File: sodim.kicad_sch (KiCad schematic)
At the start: 7 parts, among them J1 Edge_Conn_Bus_DDR5_SODIMM_1xD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, U7 AT24CS01_SOT23

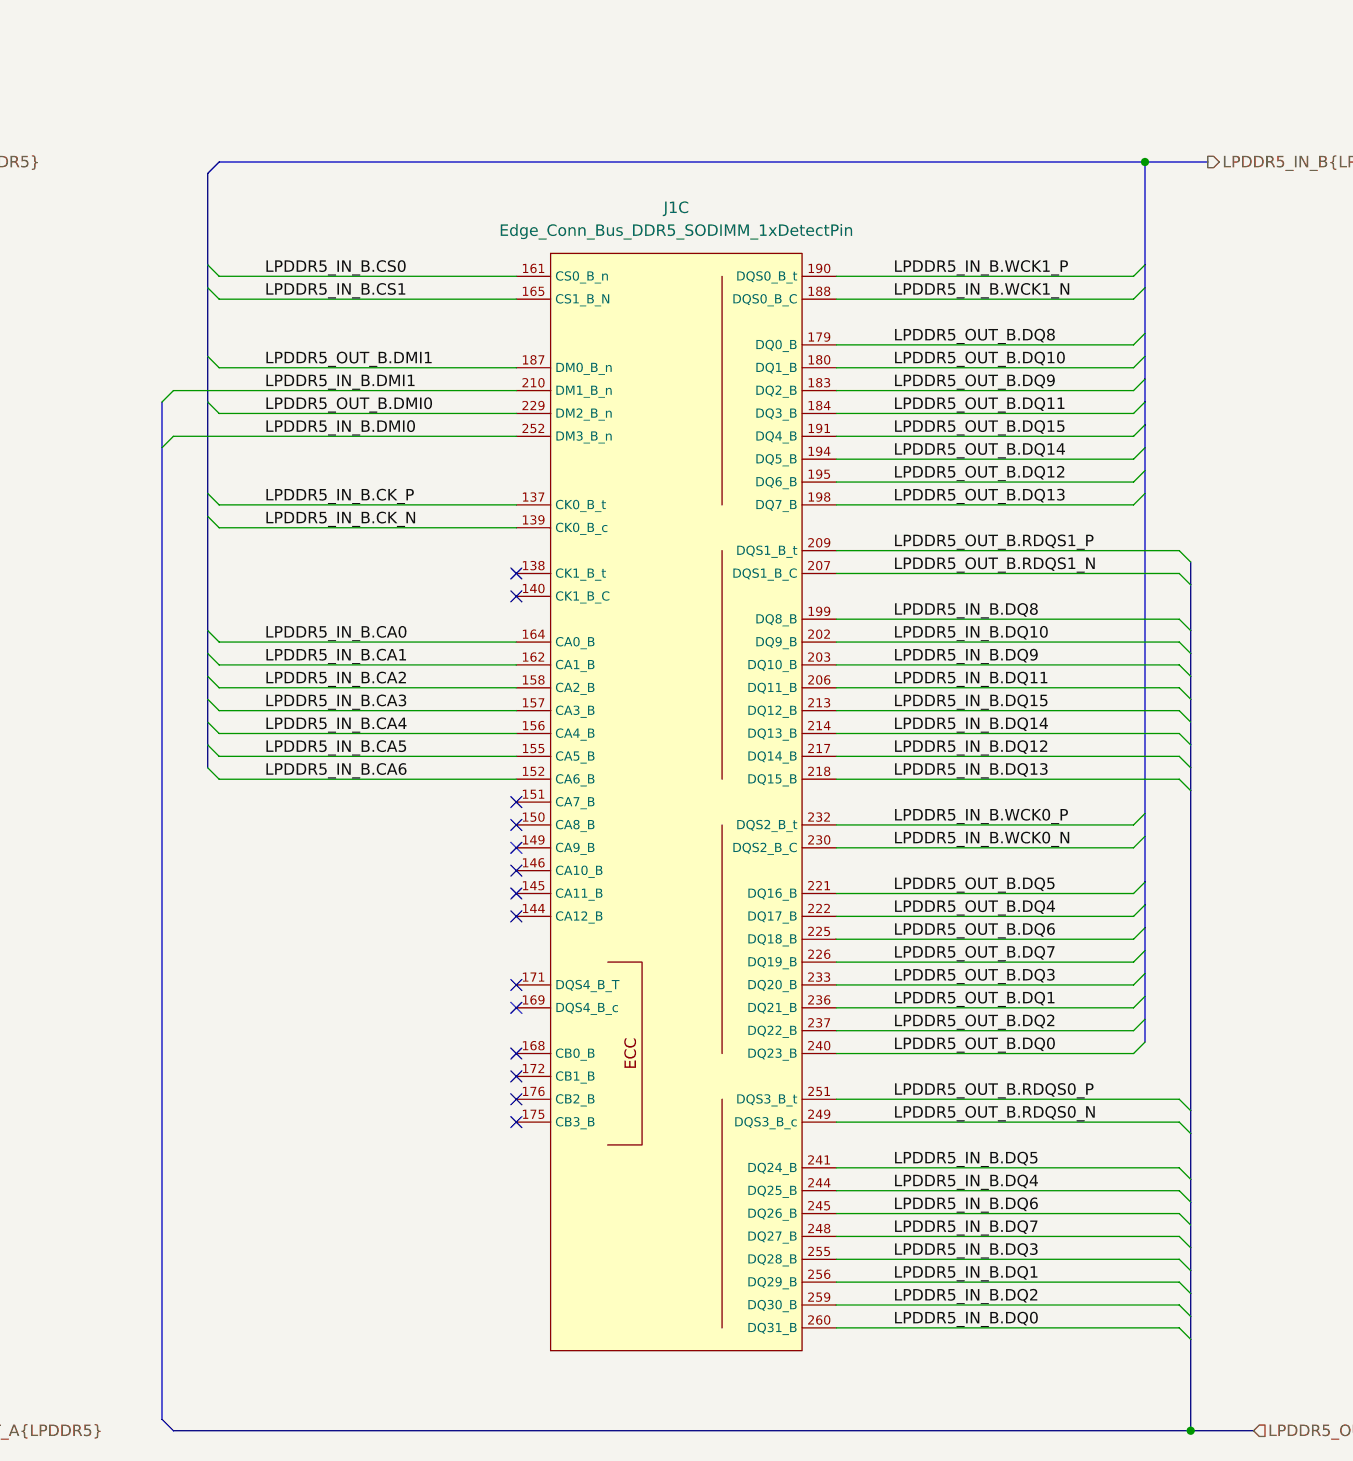
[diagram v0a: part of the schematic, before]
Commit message: [#53267] schematic: fix bus connections
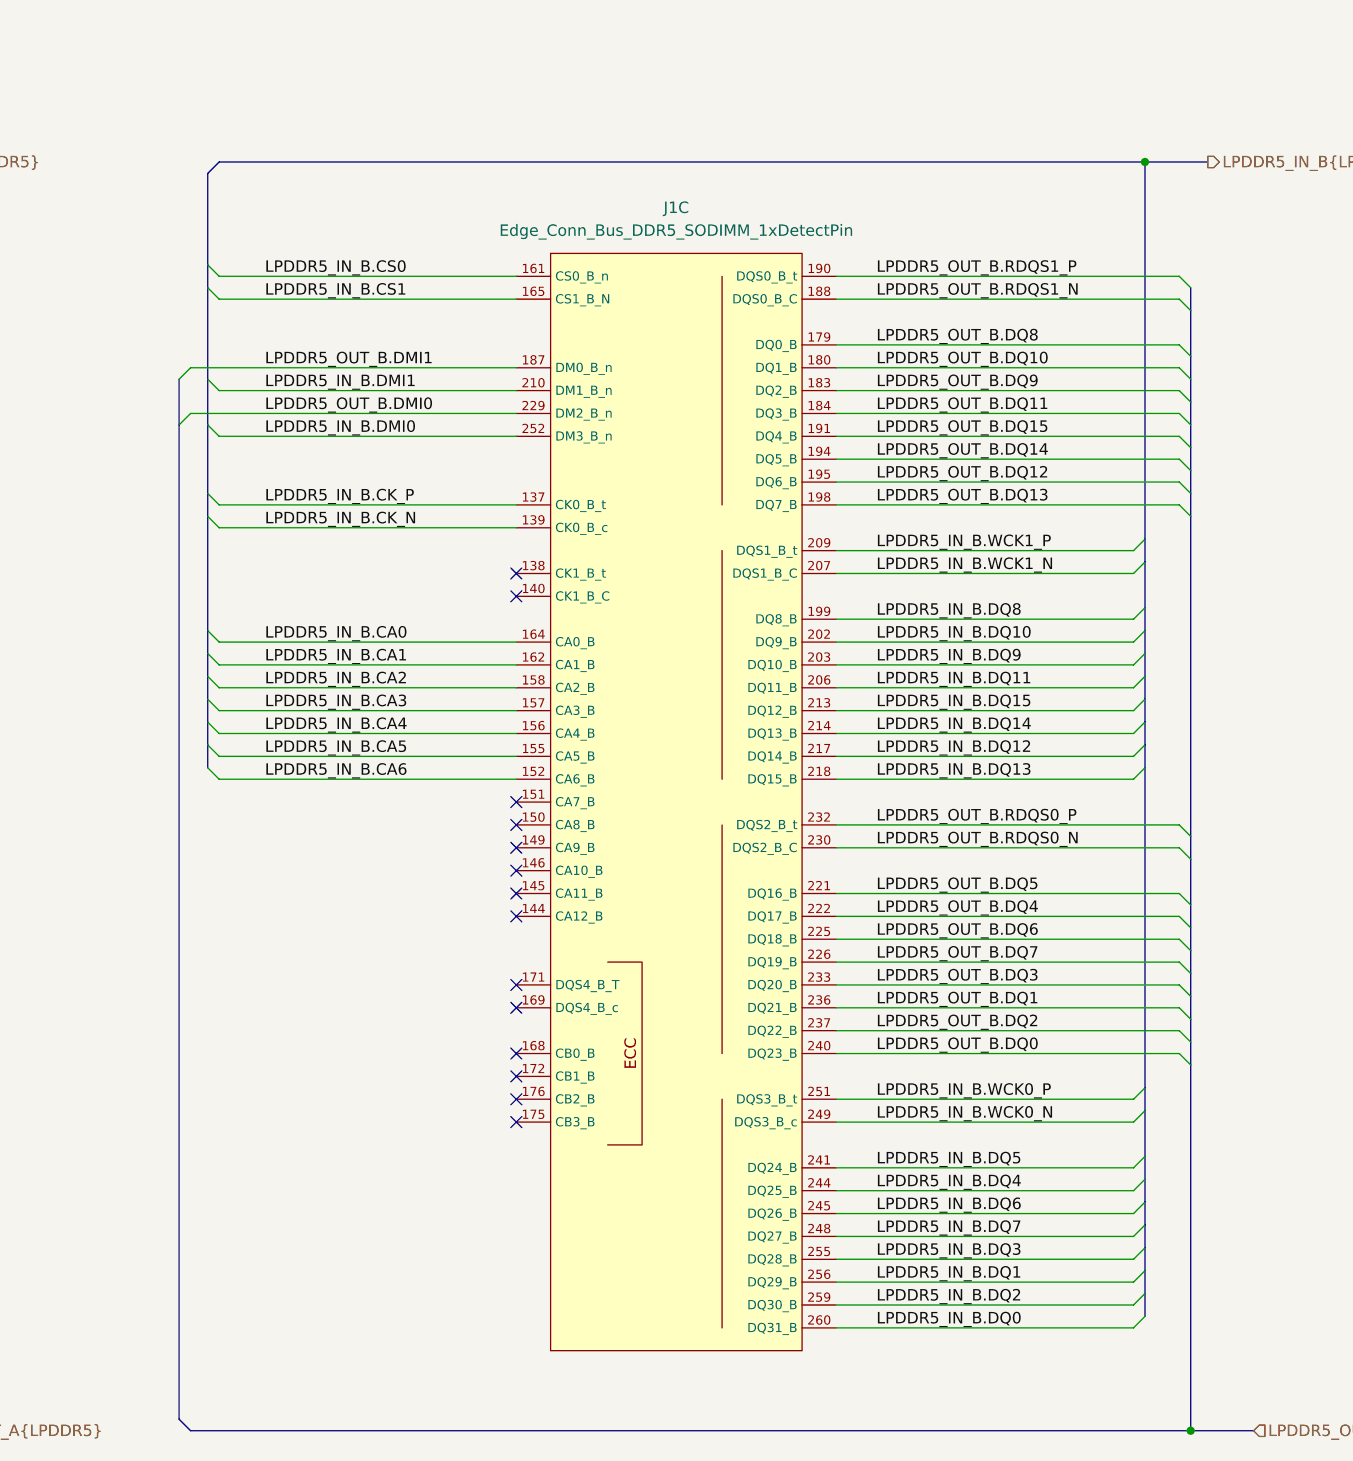
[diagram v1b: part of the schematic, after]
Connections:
- net LPDDR5_IN_B.WCK0_N: now also J1.249 (DQS3_B_c); no longer J1.230 (DQS2_B_C)
- net LPDDR5_IN_B.WCK0_P: now also J1.251 (DQS3_B_t); no longer J1.232 (DQS2_B_t)
- net LPDDR5_IN_B.WCK1_N: now also J1.207 (DQS1_B_C); no longer J1.188 (DQS0_B_C)
- net LPDDR5_IN_B.WCK1_P: now also J1.209 (DQS1_B_t); no longer J1.190 (DQS0_B_t)
- net LPDDR5_OUT_B.RDQS0_N: now also J1.230 (DQS2_B_C); no longer J1.249 (DQS3_B_c)
- net LPDDR5_OUT_B.RDQS0_P: now also J1.232 (DQS2_B_t); no longer J1.251 (DQS3_B_t)
- net LPDDR5_OUT_B.RDQS1_N: now also J1.188 (DQS0_B_C); no longer J1.207 (DQS1_B_C)
- net LPDDR5_OUT_B.RDQS1_P: now also J1.190 (DQS0_B_t); no longer J1.209 (DQS1_B_t)

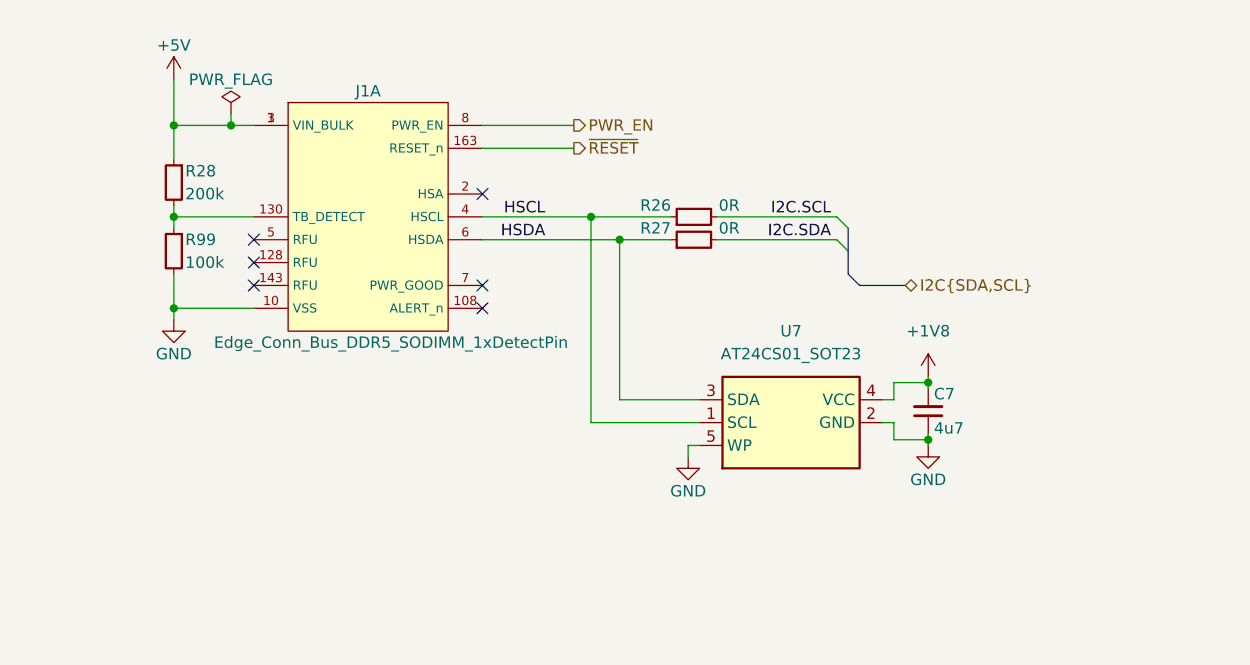
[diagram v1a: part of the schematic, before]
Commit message: [#53267] schematic: improve power supply sequencing and power good signal
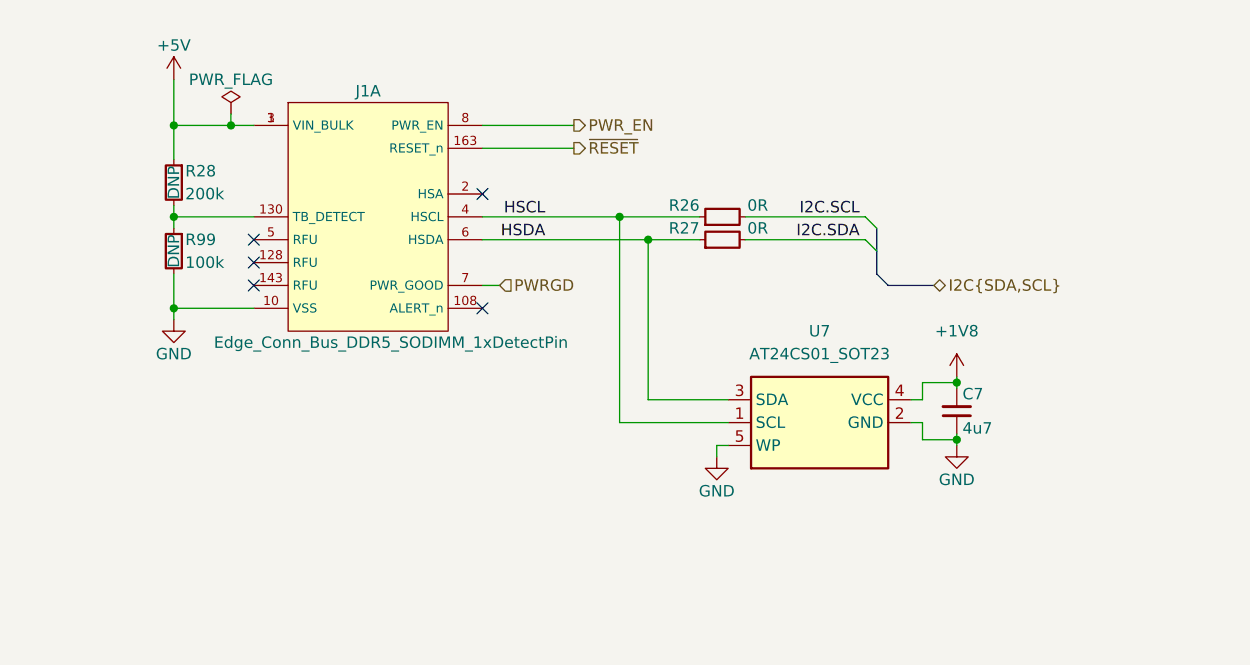
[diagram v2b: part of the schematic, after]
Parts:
- R28, R99: DNP (none) -> DNP
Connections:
- net PWRGD: now reaches J1.7 (PWR_GOOD)
- no-connect marks 34 -> 33
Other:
- moved on the sheet: C7, R26, R27, U7
